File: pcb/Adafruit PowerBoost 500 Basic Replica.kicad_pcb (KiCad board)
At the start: 2 copper layers, 32 parts, among them CN1 USBA, J1 HEADER, J2 PWR OUT, J3 Batería, Q1 MMUN2133LT1G, U1 TPS61090RSAR

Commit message: Adds missing footprint 3d models
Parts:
- L1: footprint Inductor_SMD:L_TDK_VLP8040 -> Inductor_SMD:L_Taiyo-Yuden_MD-2020
- moved FID3 16.8 mm to (139.5, 69.0)
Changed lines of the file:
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@@
     (add_net "Net-(U1-Pad2)")
+  )
+  (module Inductor_SMD:L_Taiyo-Yuden_MD-2020 (layer F.Cu)
+    (at 153 52)
+    (descr "Inductor, Taiyo Yuden, MD series, Taiyo-Yuden_MD-2020, 2.0mmx2.0mm")
+    (tags "inductor taiyo-yuden md smd")
+    (attr smd)
+    (fp_text reference L1 (at 0 -2) (layer F.SilkS)
+      (effects (font (size 1 1) (thickness 0.15)))
+    )
+    (fp_text value VLC5045-6.8uH (at 0 2.5) (layer F.Fab)
+      (effects (font (size 1 1) (thickness 0.15)))
+    )
+    (fp_text user %R (at 0 0) (layer F.Fab)
+      (effects (font (size 0.5 0.5) (thickness 0.075)))
+    )
+    (fp_line (start -1 -1) (end -1 1) (layer F.Fab) (width 0.1))
+    (fp_line (start -1 1) (end 1 1) (layer F.Fab) (width 0.1))
+    (fp_line (start 1 1) (end 1 -1) (layer F.Fab) (width 0.1))
+    (fp_line (start 1 -1) (end -1 -1) (layer F.Fab) (width 0.1))
+    (fp_line (start -1 -1.1) (end 1 -1.1) (layer F.SilkS) (width 0.12))
+    (fp_line (start -1 1.1) (end 1 1.1) (layer F.SilkS) (width 0.12))
+    (fp_line (start -1.3 -1.3) (end -1.3 1.3) (layer F.CrtYd) (width 0.05))
+    (fp_line (start -1.3 1.3) (end 1.3 1.3) (layer F.CrtYd) (width 0.05))
+    (fp_line (start 1.3 1.3) (end 1.3 -1.3) (layer F.CrtYd) (width 0.05))
+    (fp_line (start 1.3 -1.3) (end -1.3 -1.3) (layer F.CrtYd) (width 0.05))
+    (pad 2 smd rect (at 0.675 0) (size 0.65 2) (layers F.Cu F.Paste F.Mask)
+      (net 10 "Net-(L1-Pad2)"))
+    (pad 1 smd rect (at -0.675 0) (size 0.65 2) (layers F.Cu F.Paste F.Mask)
+      (net 1 +BATT))
+    (model ${KISYS3DMOD}/Inductor_SMD.3dshapes/L_Taiyo-Yuden_MD-2020.wrl
+      (at (xyz 0 0 0))
+      (scale (xyz 1 1 1))
+      (rotate (xyz 0 0 0))
+    )
+    (model /home/lorsi/Documents/CESE/DCI/tp-final-lorsi96/lib/inductor-wurth-elektronik-74437324100-1/WE_Inductor_4020.STEP
+      (at (xyz 0 0 0))
+      (scale (xyz 1 1 1))
+      (rotate (xyz 0 0 0))
+    )
   )
   (module Connector_JST:JST_EH_S2B-EH_1x02_P2.50mm_Horizontal (layer F.Cu)
@@
     )
     (fp_text value Batería (at 1.25 2.7 90) (layer F.Fab)
-      (effects (font (size 1 1) (thickness 0.15)))
-    )
-    (fp_text user %R (at 1.25 -2.6 90) (layer F.Fab)
       (effects (font (size 1 1) (thickness 0.15)))
     )
@@
     (fp_line (start -0.5 -0.7) (end 0 -1.407107) (layer F.Fab) (width 0.1))
     (fp_line (start 0 -1.407107) (end 0.5 -0.7) (layer F.Fab) (width 0.1))
+    (fp_text user %R (at 1.25 -2.6 90) (layer F.Fab)
+      (effects (font (size 1 1) (thickness 0.15)))
+    )
     (pad 2 thru_hole oval (at 2.5 0 90) (size 1.7 2) (drill 1) (layers *.Cu *.Mask)
       (net 1 +BATT))
@@
     )
     (fp_text value "PWR OUT" (at 1.25 2.7 90) (layer F.Fab)
-      (effects (font (size 1 1) (thickness 0.15)))
-    )
-    (fp_text user %R (at 1.25 -2.6 90) (layer F.Fab)
       (effects (font (size 1 1) (thickness 0.15)))
     )
@@
     (fp_line (start -0.5 -0.7) (end 0 -1.407107) (layer F.Fab) (width 0.1))
     (fp_line (start 0 -1.407107) (end 0.5 -0.7) (layer F.Fab) (width 0.1))
+    (fp_text user %R (at 1.25 -2.6 90) (layer F.Fab)
+      (effects (font (size 1 1) (thickness 0.15)))
+    )
     (pad 2 thru_hole oval (at 2.5 0 270) (size 1.7 2) (drill 1) (layers *.Cu *.Mask)
       (net 2 GND))
@@
     )
     (fp_text value USBA (at 3.5 14.5 90) (layer F.Fab)
-      (effects (font (size 1 1) (thickness 0.15)))
-    )
-    (fp_arc (start 10.07 2.71) (end 10.55 4.66) (angle -152.3426981) (layer F.CrtYd) (width 0.05))
-    (fp_arc (start -3.07 2.71) (end -3.55 0.76) (angle -152.3426981) (layer F.CrtYd) (width 0.05))
-    (fp_text user %R (at 3.5 3.7 90) (layer F.Fab)
       (effects (font (size 1 1) (thickness 0.15)))
     )
@@
     (fp_line (start -1 -2.27) (end 0 -1.27) (layer F.Fab) (width 0.1))
     (fp_line (start 0 -1.27) (end 1 -2.27) (layer F.Fab) (width 0.1))
+    (fp_arc (start 10.07 2.71) (end 10.55 4.66) (angle -152.3426981) (layer F.CrtYd) (width 0.05))
+    (fp_arc (start -3.07 2.71) (end -3.55 0.76) (angle -152.3426981) (layer F.CrtYd) (width 0.05))
+    (fp_text user %R (at 3.5 3.7 90) (layer F.Fab)
+      (effects (font (size 1 1) (thickness 0.15)))
+    )
     (pad 4 thru_hole circle (at 7 0 90) (size 1.6 1.6) (drill 0.95) (layers *.Cu *.Mask)
       (net 3 +5V))
@@
     (pad 5 thru_hole circle (at -3.07 2.71 90) (size 3 3) (drill 2.3) (layers *.Cu *.Mask)
       (net 2 GND))
-    (model ${KISYS3DMOD}/Connector_USB.3dshapes/USB_A_Molex_67643_Horizontal.wrl
-      (at (xyz 0 0 0))
-      (scale (xyz 1 1 1))
-      (rotate (xyz 0 0 0))
+    (model "/home/lorsi/Documents/CESE/DCI/tp-final-lorsi96/lib/usb-a-receptacle-tht-1/USB A Buchse THT.stp"
+      (offset (xyz 7 0 0))
+      (scale (xyz 1 1 1))
+      (rotate (xyz 0 0 -90))
     )
   )
@@
   )
   (module Fiducial:Fiducial_1mm_Mask2mm (layer F.Cu)
-    (at 126 79)
+    (at 139.5 69)
     (descr "Circular Fiducial, 1mm bare copper, 2mm soldermask opening (Level A)")
     (tags fiducial)
@@
       (at (xyz 0 0 0))
       (scale (xyz 1 1 1))
-      (rotate (xyz 0 0 0))
-    )
-  )
-  (module Inductor_SMD:L_TDK_VLP8040 (layer F.Cu)
-    (at 153 52)
-    (descr "Inductor,TDK, TDK-VLP-8040, 8.6mmx8.6mm")
-    (tags "inductor TDK VLP smd VLP8040")
-    (attr smd)
-    (fp_text reference L1 (at 0 -6.35) (layer F.SilkS)
-      (effects (font (size 1 1) (thickness 0.15)))
-    )
-    (fp_text value VLC5045-6.8uH (at 0 5.842) (layer F.Fab)
-      (effects (font (size 1 1) (thickness 0.15)))
-    )
-    (fp_circle (center 0 0) (end 3 3) (layer F.Fab) (width 0.1))
-    (fp_line (start -4.35 -4.35) (end 4.35 -4.35) (layer F.SilkS) (width 0.12))
-    (fp_line (start -4.35 4.35) (end 4.35 4.35) (layer F.SilkS) (width 0.12))
-    (fp_line (start 4.55 -4.55) (end -4.55 -4.55) (layer F.CrtYd) (width 0.05))
-    (fp_line (start 4.55 4.55) (end 4.55 -4.55) (layer F.CrtYd) (width 0.05))
-    (fp_line (start -4.55 4.55) (end 4.55 4.55) (layer F.CrtYd) (width 0.05))
-    (fp_line (start -4.55 -4.55) (end -4.55 4.55) (layer F.CrtYd) (width 0.05))
-    (fp_line (start 3.5 -3.5) (end 2.4 -3.5) (layer F.Fab) (width 0.1))
-    (fp_line (start 3.5 -3.5) (end 3.5 -2.4) (layer F.Fab) (width 0.1))
-    (fp_line (start -3.5 3.5) (end -2.4 3.5) (layer F.Fab) (width 0.1))
-    (fp_line (start -3.5 2.4) (end -3.5 3.5) (layer F.Fab) (width 0.1))
-    (fp_line (start 3.5 2.4) (end 3.5 3.5) (layer F.Fab) (width 0.1))
-    (fp_line (start 3.5 3.5) (end 2.4 3.5) (layer F.Fab) (width 0.1))
-    (fp_line (start -3.5 -2.4) (end -3.5 -3.5) (layer F.Fab) (width 0.1))
-    (fp_line (start -3.5 -3.5) (end -2.4 -3.5) (layer F.Fab) (width 0.1))
-    (fp_text user %R (at 0 0) (layer F.Fab)
-      (effects (font (size 1 1) (thickness 0.15)))
-    )
-    (pad 1 smd rect (at -2.35 0) (size 3.3 8.2) (layers F.Cu F.Paste F.Mask)
-      (net 1 +BATT))
-    (pad 2 smd rect (at 2.35 0) (size 3.3 8.2) (layers F.Cu F.Paste F.Mask)
-      (net 10 "Net-(L1-Pad2)"))
-    (model ${KISYS3DMOD}/Inductor_SMD.3dshapes/L_TDK_VLP8040.wrl
-      (at (xyz 0 0 0))
-      (scale (xyz 1 1 1))

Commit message: Agrega Ruteo
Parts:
- C1, C2, C3: footprint Capacitor_SMD:C_0805_2012Metric -> Capacitor_SMD:C_0805_2012Metric_Pad1.18x1.45mm_HandSolder
- C4: footprint Capacitor_SMD:C_1206_3216Metric -> Capacitor_SMD:C_1210_3225Metric_Pad1.33x2.70mm_HandSolder
- D1, D2: footprint LED_SMD:LED_0805_2012Metric -> LED_SMD:LED_0805_2012Metric_Pad1.15x1.40mm_HandSolder
- L1: footprint Inductor_SMD:L_Taiyo-Yuden_MD-2020 -> Inductor_SMD:L_Taiyo-Yuden_NR-40xx_HandSoldering
- R1, R10, R11, R2, R3, R4, R5, R6, R7, R8, R9: footprint Resistor_SMD:R_0805_2012Metric -> Resistor_SMD:R_0805_2012Metric_Pad1.20x1.40mm_HandSolder
- moved FID3 32.9 mm to (172.0, 74.0)
- moved D2 18.0 mm to (144.0, 65.0), turned to 90 degrees
- moved R10 17.3 mm to (161.0, 74.0)
- moved J2 15.6 mm to (164.0, 60.2)
- moved C1 14.3 mm to (143.0, 48.0), turned to 0 degrees
- moved R4 14.0 mm to (144.0, 70.0), turned to 90 degrees
- moved J1 13.7 mm to (150.5, 47.5), turned to 90 degrees
- moved CN1 13.6 mm to (160.0, 65.0)
- moved C3 13.0 mm to (151.0, 71.0)
- moved J3 11.6 mm to (140.0, 62.5)
- moved R11 10.7 mm to (160.0, 71.0)
- moved H1 10.6 mm to (137.0, 50.0)
- moved H3 10.6 mm to (167.0, 50.0)
- moved R6 9.96 mm to (144.0, 61.0), turned to 270 degrees
- moved H4 8.06 mm to (167.0, 72.0)
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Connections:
- J1 pad 3: /ENABLE -> /LBO
- J1 pad 4: /LBO -> /ENABLE
- J1 pad 5: GND -> +5V
- J1 pad 6: +5V -> GND
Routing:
- net +5V: track 0.00 -> 83.6 mm
- net GND: track 0.00 -> 81.5 mm, vias 0 -> 2
- net /LBO: track 0.00 -> 43.7 mm, vias 0 -> 1
- net +BATT: track 0.00 -> 41.3 mm
- net /ENABLE: track 0.00 -> 35.0 mm, vias 0 -> 1
- net Net-(CN1-Pad2): track 0.00 -> 17.7 mm
- net Net-(CN1-Pad3): track 0.00 -> 14.3 mm
- net Net-(R4-Pad2): track 0.00 -> 12.7 mm
- net Net-(R2-Pad2): track 0.00 -> 12.4 mm
- net Net-(L1-Pad2): track 0.00 -> 12.3 mm
- net Net-(Q1-Pad3): track 0.00 -> 6.24 mm
- net Net-(D1-Pad1): track 0.00 -> 2.97 mm
- net Net-(D2-Pad2): track 0.00 -> 1.98 mm
- added copper zone on B.Cu, net GND
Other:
- board outline added: 44 x 32 mm
- net class Default: clearance 0.8 -> 0.3; trace_width 0.8 -> 0.7
- rule trace_clearance: 0.8 -> 0.3

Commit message: Applies Diego Corrections
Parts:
- removed FID2: U1 FID, Fiducial:Fiducial_0.5mm_Mask1mm
- J2: footprint Connector_JST:JST_EH_S2B-EH_1x02_P2.50mm_Horizontal -> dci_lorsi:JST_EH_S2B-EH_1x02_P2.50mm_Horizontal
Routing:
- net Net-(R4-Pad2): track 12.7 -> 14.2 mm
- net Net-(L1-Pad2): track 12.3 -> 13.0 mm

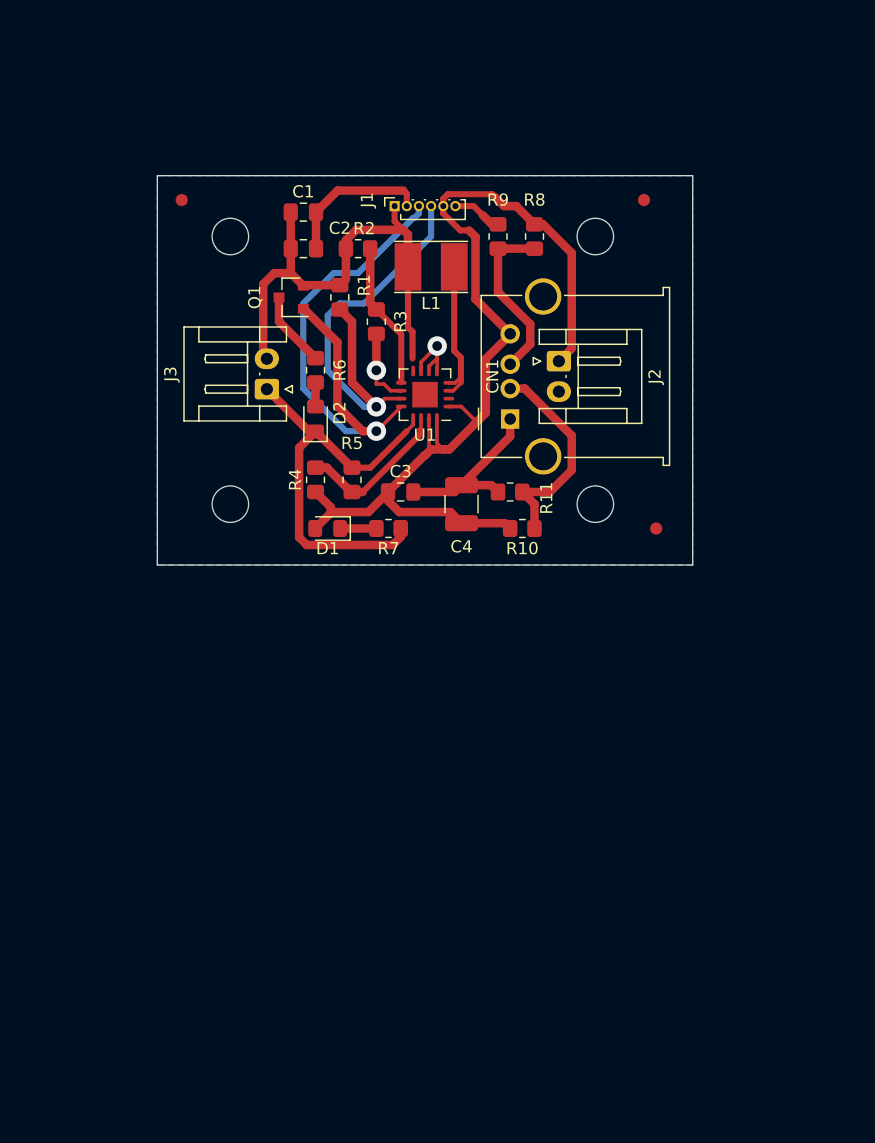
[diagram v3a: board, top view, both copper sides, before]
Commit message: Cambios de acuerdo a checks del excel
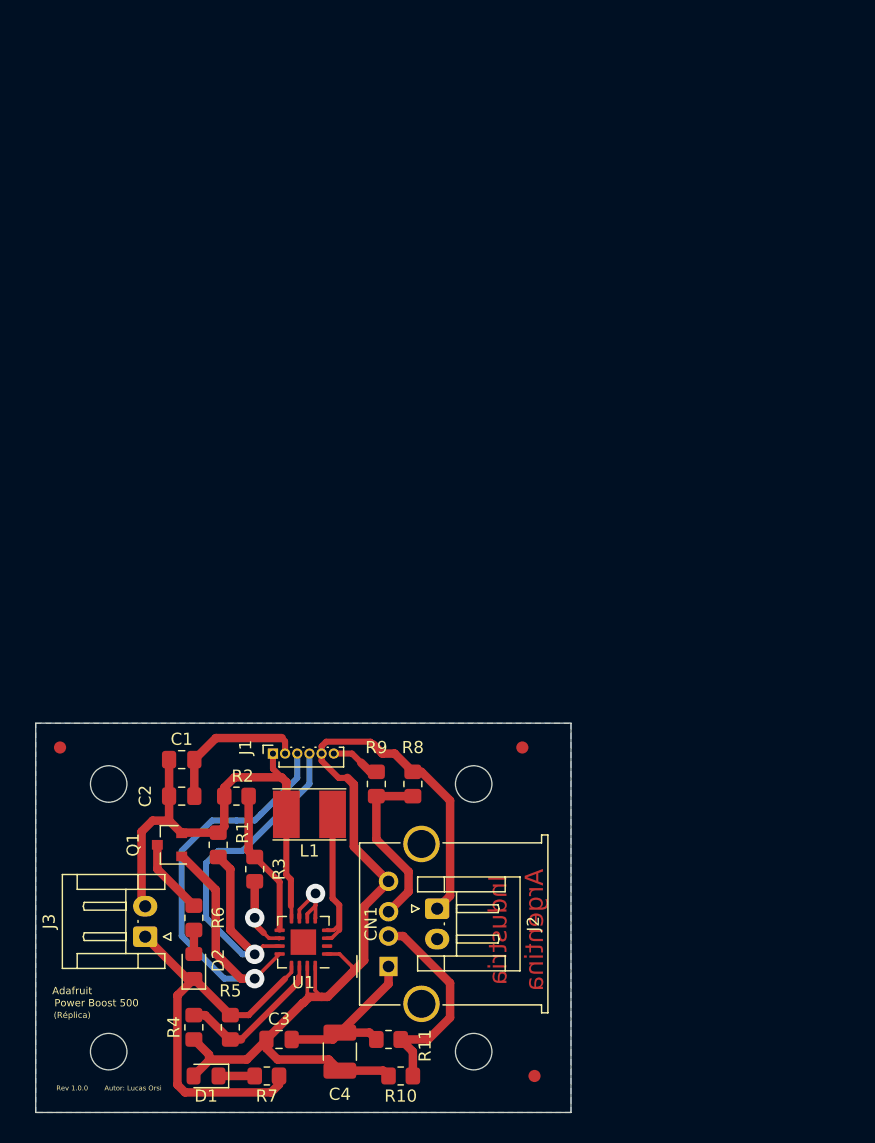
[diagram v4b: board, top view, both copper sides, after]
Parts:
- moved C1 46.1 mm to (133.0, 93.0)
- moved C2 46.1 mm to (133.0, 96.0)
- moved C3 46.1 mm to (141.0, 116.0)
- moved C4 46.1 mm to (146.0, 117.0)
- moved CN1 46.1 mm to (150.0, 110.0)
- moved D1 46.1 mm to (135.0, 119.0)
- moved D2 46.1 mm to (134.0, 110.0)
- moved FID1 46.1 mm to (123.0, 92.0)
- moved FID3 46.1 mm to (162.0, 119.0)
- moved FID4 46.1 mm to (161.0, 92.0)
- moved H1 46.1 mm to (127.0, 95.0)
- moved H2 46.1 mm to (127.0, 117.0)
- moved H3 46.1 mm to (157.0, 95.0)
- moved H4 46.1 mm to (157.0, 117.0)
- moved J1 46.1 mm to (140.5, 92.5)
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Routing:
- net +BATT: track 41.1 -> 42.1 mm
- net /LBO: track 43.7 -> 44.6 mm
- net GND: track 81.3 -> 80.6 mm
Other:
- board text added: "(Réplica)"
- board text added: "Adafruit"
- board text added: "Argentina"
- board text added: "Autor: Lucas Orsi"
- board text added: "Fabricante de Referencia: Ernesto Mayer S.A."
- board text added: "Grillas: 1,000 mm & 0.500 mm"
- board text added: "Industria"
- board text added: "Power Boost 500"
- board text added: "Rev 1.0.0"
- board text added: "Terminación superficial: HASL plomo-estaño"

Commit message: Terminado
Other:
- board text added: "Ancho de Pistas: 0.7mm, 0.5mm, 0.3mm"
- board text added: "Clearance 0,3mm"
- board text added: "Espesor 1.6mm"
- board text added: "Espesor de Cobre: 1oz"
- board text added: "Número de Capas: 2"
- board text added: "Terminación superficial: HASL"
- board text added: "Vias 1.6mm/0.8mm"
- board text removed: "Terminación superficial: HASL plomo-estaño"
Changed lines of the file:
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@@
   (general
     (thickness 1.6)
-    (drawings 16)
+    (drawings 37)
     (tracks 192)
     (zones 0)
@@
     )
   )
-  (gr_text Argentina (at 162 107 90) (layer F.Cu)
-    (effects (font (size 1.5 1.5) (thickness 0.3)) (justify mirror))
-  )
-  (gr_text "Industria " (at 159 107 90) (layer F.Cu)
-    (effects (font (size 1.5 1.5) (thickness 0.3)) (justify mirror))
+  (gr_line (start 181 91) (end 182 91) (layer F.CrtYd) (width 0.05))
+  (gr_line (start 181 121) (end 181 91) (layer F.CrtYd) (width 0.05))
+  (gr_line (start 222 121) (end 181 121) (layer F.CrtYd) (width 0.05))
+  (gr_line (start 222 91) (end 222 121) (layer F.CrtYd) (width 0.05))
+  (gr_line (start 221 91) (end 222 91) (layer F.CrtYd) (width 0.05))
+  (gr_line (start 182 91) (end 221 91) (layer F.CrtYd) (width 0.05))
+  (gr_line (start 183 119) (end 183 109) (layer F.CrtYd) (width 0.05))
+  (gr_line (start 220 119) (end 183 119) (layer F.CrtYd) (width 0.05))
+  (gr_line (start 220 109) (end 220 119) (layer F.CrtYd) (width 0.05))
+  (gr_line (start 183 109) (end 220 109) (layer F.CrtYd) (width 0.05))
+  (gr_line (start 183 93) (end 184 93) (layer F.CrtYd) (width 0.05))
+  (gr_line (start 183 105) (end 183 93) (layer F.CrtYd) (width 0.05))
+  (gr_line (start 220 105) (end 183 105) (layer F.CrtYd) (width 0.05))
+  (gr_line (start 220 93) (end 220 105) (layer F.CrtYd) (width 0.05))
+  (gr_line (start 184 93) (end 220 93) (layer F.CrtYd) (width 0.05))
+  (gr_text "Espesor 1.6mm" (at 190.166667 101) (layer F.CrtYd)
+    (effects (font (size 1 1) (thickness 0.15)))
+  )
+  (gr_text "Número de Capas: 2" (at 192.190476 103) (layer F.CrtYd)
+    (effects (font (size 1 1) (thickness 0.15)))
+  )
+  (gr_text "Espesor de Cobre: 1oz" (at 193 99) (layer Dwgs.User)
+    (effects (font (size 1 1) (thickness 0.15)))
+  )
+  (gr_text "Ancho de Pistas: 0.7mm, 0.5mm, 0.3mm" (at 200.095238 117) (layer Dwgs.User)
+    (effects (font (size 1 1) (thickness 0.15)))
+  )
+  (gr_text "Vias 1.6mm/0.8mm" (at 192 115) (layer Dwgs.User)
+    (effects (font (size 1 1) (thickness 0.15)))
+  )
+  (gr_text "Clearance 0,3mm" (at 191.142857 113) (layer Dwgs.User)
+    (effects (font (size 1 1) (thickness 0.15)))
+  )
+  (gr_text Argentina (at 163 96 90) (layer F.Cu)
+    (effects (font (size 0.7 0.7) (thickness 0.175)))
+  )
+  (gr_text "Industria " (at 162 96 90) (layer F.Cu)
+    (effects (font (size 0.7 0.7) (thickness 0.175)))
   )
   (gr_text "Autor: Lucas Orsi" (at 129 120) (layer F.SilkS)
@@
     (effects (font (size 0.6 0.6) (thickness 0.15)))
   )
-  (gr_text "Grillas: 1,000 mm & 0.500 mm" (at 184 95) (layer Dwgs.User)
+  (gr_text "Grillas: 1,000 mm & 0.500 mm" (at 196.666667 111) (layer Dwgs.User)
     (effects (font (size 1 1) (thickness 0.15)))
   )
-  (gr_text "Terminación superficial: HASL plomo-estaño" (at 189 93) (layer Dwgs.User)
+  (gr_text "Terminación superficial: HASL" (at 195.642857 97) (layer Dwgs.User)
     (effects (font (size 1 1) (thickness 0.15)))
   )
-  (gr_text "Fabricante de Referencia: Ernesto Mayer S.A." (at 189 91) (layer Dwgs.User)
+  (gr_text "Fabricante de Referencia: Ernesto Mayer S.A." (at 201.571428 95) (layer Dwgs.User)
     (effects (font (size 1 1) (thickness 0.15)))
   )

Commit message: Ultimo commit post presentación
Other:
- board size 44 x 32 mm -> 45 x 33 mm
- board text added: "5V"
- board text added: "BAT"
- board text added: "EN"
- board text added: "GND"
- board text added: "LBO"
- board text removed: "Espesor de Cobre: 1oz"
- board text removed: "Número de Capas: 2"
